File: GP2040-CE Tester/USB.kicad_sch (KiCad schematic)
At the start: 1 part, among them P1 USB_C_Plug

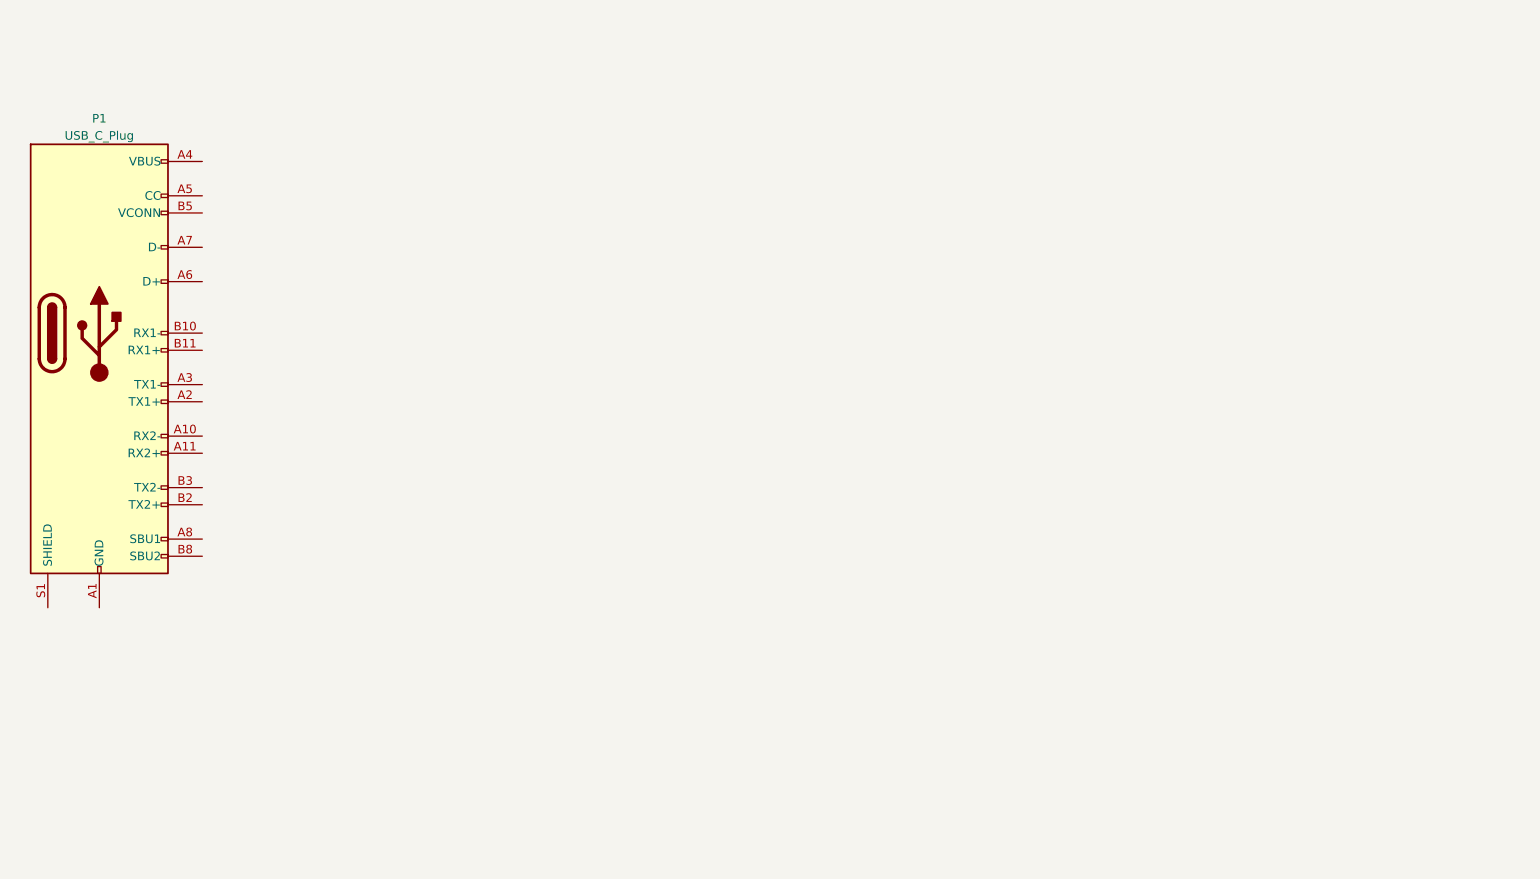
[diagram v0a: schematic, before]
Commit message: adding most of the components, and schematic connections
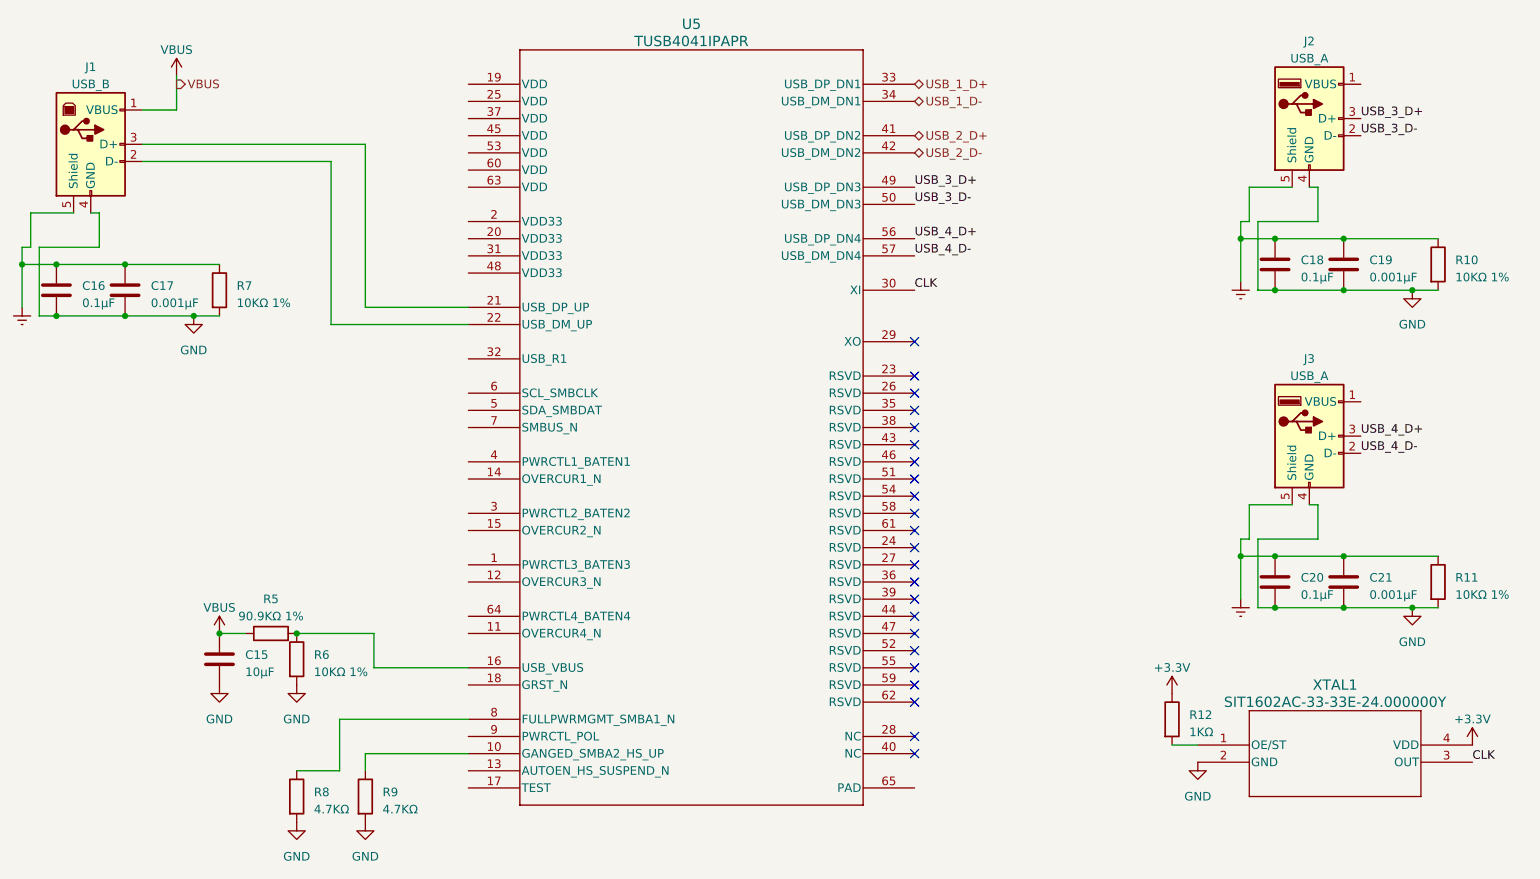
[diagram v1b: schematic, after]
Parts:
- removed P1: USB_C_Plug, Connector_USB:USB_C_Plug_Molex_105444, symbol Connector:USB_C_Plug
- added C15: 10μF, Capacitor_SMD:C_0603_1608Metric, symbol Device:C
- added C16, C18, C20: 0.1μF, Capacitor_SMD:C_0603_1608Metric, symbol Device:C
- added C17, C19, C21: 0.001μF, Capacitor_SMD:C_0603_1608Metric, symbol Device:C
- added J1: USB_B, Connector_USB:USB_B_Lumberg_2411_02_Horizontal, symbol Connector:USB_B
- added J2, J3: USB_A, Connector_USB:USB_A_Molex_67643_Horizontal, symbol Connector:USB_A
- added R10, R11, R7: 10KΩ 1%, Resistor_SMD:R_0402_1005Metric, symbol Device:R
- added R12: 1KΩ, Resistor_SMD:R_0603_1608Metric, symbol Device:R
- added R5: 90.9KΩ 1%, Resistor_SMD:R_0603_1608Metric, symbol Device:R
- added R6: 10KΩ 1%, Resistor_SMD:R_0603_1608Metric, symbol Device:R
- added R8, R9: 4.7KΩ, Resistor_SMD:R_0603_1608Metric, symbol Device:R
- added U5: TUSB4041IPAPR, GP2040-CE-Tester:TUSB4041I-Q1, symbol GP2040-CE-Tester:TUSB4041IPAPR
- added XTAL1: SIT1602AC-33-33E-24.000000Y, GP2040-CE-Tester:SIT1602, symbol GP2040-CE-Tester:SIT1602AC-33-33E-24.000000Y
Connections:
- new net: R9.1, U5.10 (GANGED_SMBA2_HS_UP)
- new net: R5.2, R6.1, U5.16 (USB_VBUS)
- new net: J1.3 (D+), U5.21 (USB_DP_UP)
- new net: J1.2 (D-), U5.22 (USB_DM_UP)
- new net: R8.1, U5.8 (FULLPWRMGMT_SMBA1_N)
- new net: R12.2, XTAL1.1 (OE/ST)
- new net +3.3V: R12.1, XTAL1.4 (VDD)
- new net CLK: U5.30 (XI), XTAL1.3 (OUT)
- new net Earth: C16.1, C17.1, C18.1, C19.1, C20.1, C21.1, J1.5 (Shield), J2.5 (Shield), J3.5 (Shield), R10.1, R11.1, R7.1
- new net GND: C15.2, C16.2, C17.2, C18.2, C19.2, C20.2, C21.2, J1.4 (GND), J2.4 (GND), J3.4 (GND), R10.2, R11.2, R6.2, R7.2, R8.2, R9.2, XTAL1.2 (GND)
- new net USB_1_D+: U5.33 (USB_DP_DN1)
- new net USB_1_D-: U5.34 (USB_DM_DN1)
- new net USB_2_D+: U5.41 (USB_DP_DN2)
- new net USB_2_D-: U5.42 (USB_DM_DN2)
- new net USB_3_D+: J2.3 (D+), U5.49 (USB_DP_DN3)
- new net USB_3_D-: J2.2 (D-), U5.50 (USB_DM_DN3)
- new net USB_4_D+: J3.3 (D+), U5.56 (USB_DP_DN4)
- new net USB_4_D-: J3.2 (D-), U5.57 (USB_DM_DN4)
- new net VBUS: C15.1, J1.1 (VBUS), R5.1
- no-connect marks 0 -> 23

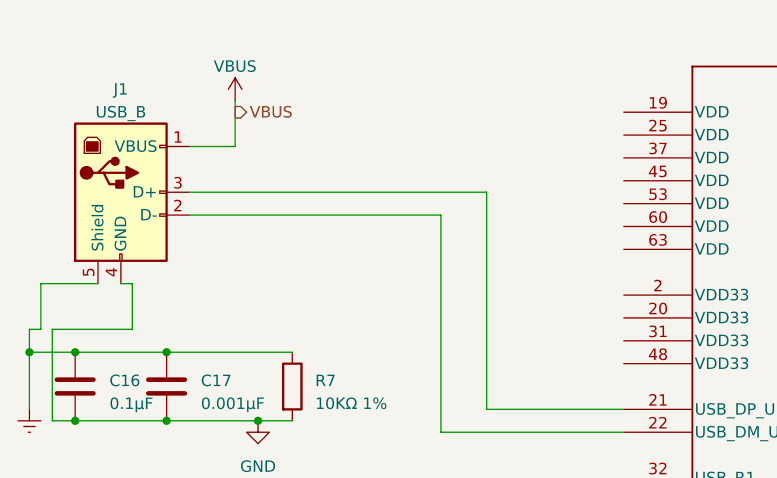
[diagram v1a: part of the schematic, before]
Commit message: adding most of the components, and schematic connections
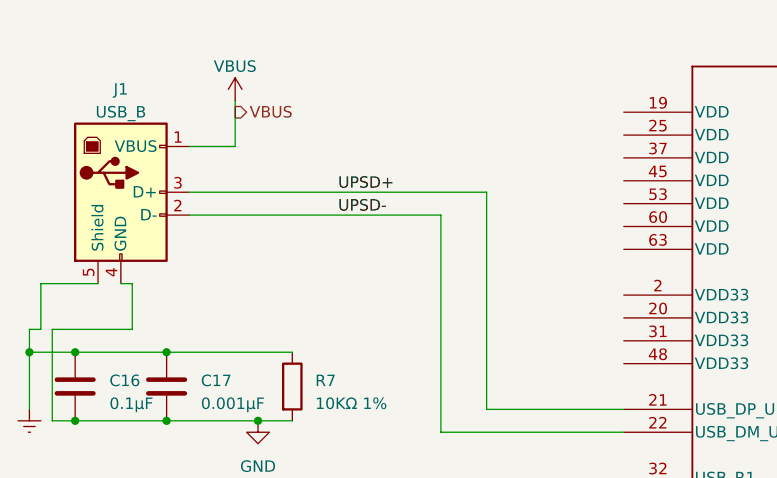
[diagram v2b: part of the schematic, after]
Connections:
- net UPSD+: now reaches J1.3 (D+), U5.21 (USB_DP_UP)
- net UPSD-: now reaches J1.2 (D-), U5.22 (USB_DM_UP)
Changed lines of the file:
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@@
+    (effects (font (size 1.27 1.27)) (justify left bottom))
+  )
+  (label "UPSD-" (at 60.96 36.83 0) (fields_autoplaced)
     (effects (font (size 1.27 1.27)) (justify left bottom))
   )
@@
     (effects (font (size 1.27 1.27)) (justify left bottom))
   )
+  (label "UPSD+" (at 60.96 34.29 0) (fields_autoplaced)
+    (effects (font (size 1.27 1.27)) (justify left bottom))
+  )
